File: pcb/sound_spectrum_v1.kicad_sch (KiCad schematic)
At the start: 0 parts

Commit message: feat: form pcb board as credit card-sized
feat: add esd protection ic to USB singals

fix: bug with nrst button

fix: bug with microphone connection in schematic

chore: added custom rules for board in jlcpcb
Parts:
- added C1, C12, C13, C14, C3, C6, C7, C8: 100nF, Capacitor_SMD:C_0805_2012Metric_Pad1.18x1.45mm_HandSolder, symbol Device:C
- added C10, C11: 10uF, Capacitor_SMD:C_0805_2012Metric_Pad1.18x1.45mm_HandSolder, symbol Device:C
- added C2, C4, C5, C9: 1uF, Capacitor_SMD:C_0805_2012Metric_Pad1.18x1.45mm_HandSolder, symbol Device:C
- added D2: LED, LED_SMD:LED_0805_2012Metric_Pad1.15x1.40mm_HandSolder, symbol Device:LED
- added FB1: 4.7uH, Inductor_SMD:L_0805_2012Metric_Pad1.05x1.20mm_HandSolder, symbol Device:FerriteBead
- added J1: SWD_CONN, Connector_PinHeader_2.54mm:PinHeader_2x03_P2.54mm_Vertical, symbol Connector_Generic:Conn_02x03_Counter_Clockwise
- added J2: Conn_02x10_Counter_Clockwise, Connector_PinHeader_2.54mm:PinHeader_2x10_P2.54mm_Vertical, symbol Connector_Generic:Conn_02x10_Counter_Clockwise
- added JP1: Jumper_3_Bridged12, Jumper:SolderJumper-3_P1.3mm_Bridged2Bar12_Pad1.0x1.5mm, symbol Jumper:Jumper_3_Bridged12
- added MK1-L1, MK1-R1: ICS-43434, Sensor_Audio:InvenSense_ICS-43434-6_3.5x2.65mm, symbol Sensor_Audio:ICS-43434
- added P1: USB_C_Plug_USB2.0, Connector_USB:USB_C_Receptacle_GCT_USB4085, symbol Connector:USB_C_Plug_USB2.0
- added R1: 10k, Resistor_SMD:R_0805_2012Metric_Pad1.20x1.40mm_HandSolder, symbol Device:R
- added R3: 5.1k, Resistor_SMD:R_0805_2012Metric_Pad1.20x1.40mm_HandSolder, symbol Device:R
- added R4: 1k, Resistor_SMD:R_0805_2012Metric_Pad1.20x1.40mm_HandSolder, symbol Device:R
- added R5, R6: 4.7k, Resistor_SMD:R_0805_2012Metric_Pad1.20x1.40mm_HandSolder, symbol Device:R
- added SW2: SW_DPST_x2, Button_Switch_THT:SW_PUSH_6mm, symbol Switch:SW_DPST_x2
- added U1: STM32G473CBTx, Package_QFP:LQFP-48_7x7mm_P0.5mm, symbol user_defined_libs:STM32G473CBTx
- added U2: AP2112K-3.3, Package_TO_SOT_SMD:SOT-23-5, symbol Regulator_Linear:AP2112K-3.3
- added U3: USBLC6-2SC6, Package_TO_SOT_SMD:SOT-23-6, symbol Power_Protection:USBLC6-2SC6
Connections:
- new net: D2.2 (A), R4.1
- new net: R1.1, U2.3 (EN)
- new net: P1.A5 (CC), R3.1
- new net +3.3V: C1.1, C10.1, C12.1, C13.1, C2.1, C3.1, C4.1, C5.1, C6.1, C7.1, C8.1, C9.1, FB1.1, FB1.2, J1.1 (Pin_1), J2.1 (Pin_1), J2.2 (Pin_2), J2.3 (Pin_3), JP1.3 (B), MK1-L1.5 (VDD), MK1-R1.2 (LR), MK1-R1.5 (VDD), R4.2, R5.2, R6.2, U1.1 (VBAT), U1.20 (VREF+), U1.21 (VDDA), U1.24 (VDD), U1.36 (VDD), U1.48 (VDD), U2.5 (VOUT)
- new net +5V: J2.10 (Pin_10), J2.8 (Pin_8), J2.9 (Pin_9)
- new net BOOT0: JP1.2 (C), U1.45 (PB8)
- new net GND: C1.2, C10.2, C11.2, C12.2, C13.2, C14.1, C2.2, C3.2, C4.2, C5.2, C6.2, C7.2, C8.2, C9.2, D2.1 (K), J1.3 (Pin_3), J2.11 (Pin_11), J2.4 (Pin_4), J2.5 (Pin_5), J2.6 (Pin_6), J2.7 (Pin_7), JP1.1 (A), MK1-L1.2 (LR), MK1-L1.3 (GND), MK1-R1.3 (GND), P1.A1 (GND), P1.A12 (GND), P1.B1 (GND), P1.B12 (GND), P1.S1 (SHIELD), R3.2, SW2.1 (A), U1.19 (VSSA), U1.23 (VSS), U1.35 (VSS), U1.47 (VSS), U2.2 (GND), U3.2 (GND)
- new net I2C_SCL: J2.19 (Pin_19), R6.1, U1.39 (PA15)
- new net I2C_SDA: J2.20 (Pin_20), R5.1, U1.44 (PB7)
- new net I2S_CLK: U1.27 (PB13)
- new net I2S_SCK: MK1-L1.4 (SCK), MK1-R1.4 (SCK)
- new net I2S_SD: MK1-L1.6 (SD), MK1-R1.6 (SD), U1.29 (PB15)
- new net I2S_WS: MK1-L1.1 (WS), MK1-R1.1 (WS), U1.26 (PB12)
- new net NRST: C14.2, J1.5 (Pin_5), SW2.2 (B), U1.7 (PG10)
- new net SPI_MISO: J2.17 (Pin_17), U1.14 (PA6)
- new net SPI_MOSI: J2.18 (Pin_18), U1.15 (PA7)
- new net SPI_NSS: J2.15 (Pin_15), U1.12 (PA4)
- new net SPI_SCK: J2.16 (Pin_16), U1.13 (PA5)
- new net SWCLK: J1.2 (Pin_2), U1.38 (PA14)
- new net SWDIO: J1.4 (Pin_4), U1.37 (PA13)
- new net SWO: J1.6 (Pin_6), U1.40 (PB3)
- new net UART_CK: J2.14 (Pin_14), U1.30 (PA8)
- new net UART_RX: J2.12 (Pin_12), U1.32 (PA10)
- new net UART_TX: J2.13 (Pin_13), U1.31 (PA9)
- new net USB_DM: U1.33 (PA11), U3.1 (I/O1)
- new net USB_DM_EXT: P1.A7 (D-), U3.6 (I/O1)
- new net USB_DP: U1.34 (PA12), U3.3 (I/O2)
- new net USB_DP_EXT: P1.A6 (D+), U3.4 (I/O2)
- new net VBUS: C11.1, P1.A4 (VBUS), P1.A9 (VBUS), P1.B4 (VBUS), P1.B9 (VBUS), R1.2, U2.1 (VIN), U3.5 (VBUS)
- no-connect marks 0 -> 1
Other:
- company: (none) -> Petros Athanaselis
- title: (none) -> Sound Analysis PCB

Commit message: chore: further tracing
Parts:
- JP1: value Jumper_3_Bridged12 -> BOOT_SELECT
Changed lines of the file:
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@@
 		(on_board yes)
 		(dnp no)
-		(fields_autoplaced yes)
 		(property "Reference" "C12"
 			(at 26.67 167.6399 0)
@@
 			)
 		)
-		(property "Value" "Jumper_3_Bridged12"
+		(property "Value" "BOOT_SELECT"
 			(at 29.21 93.9799 90)
 			(effects

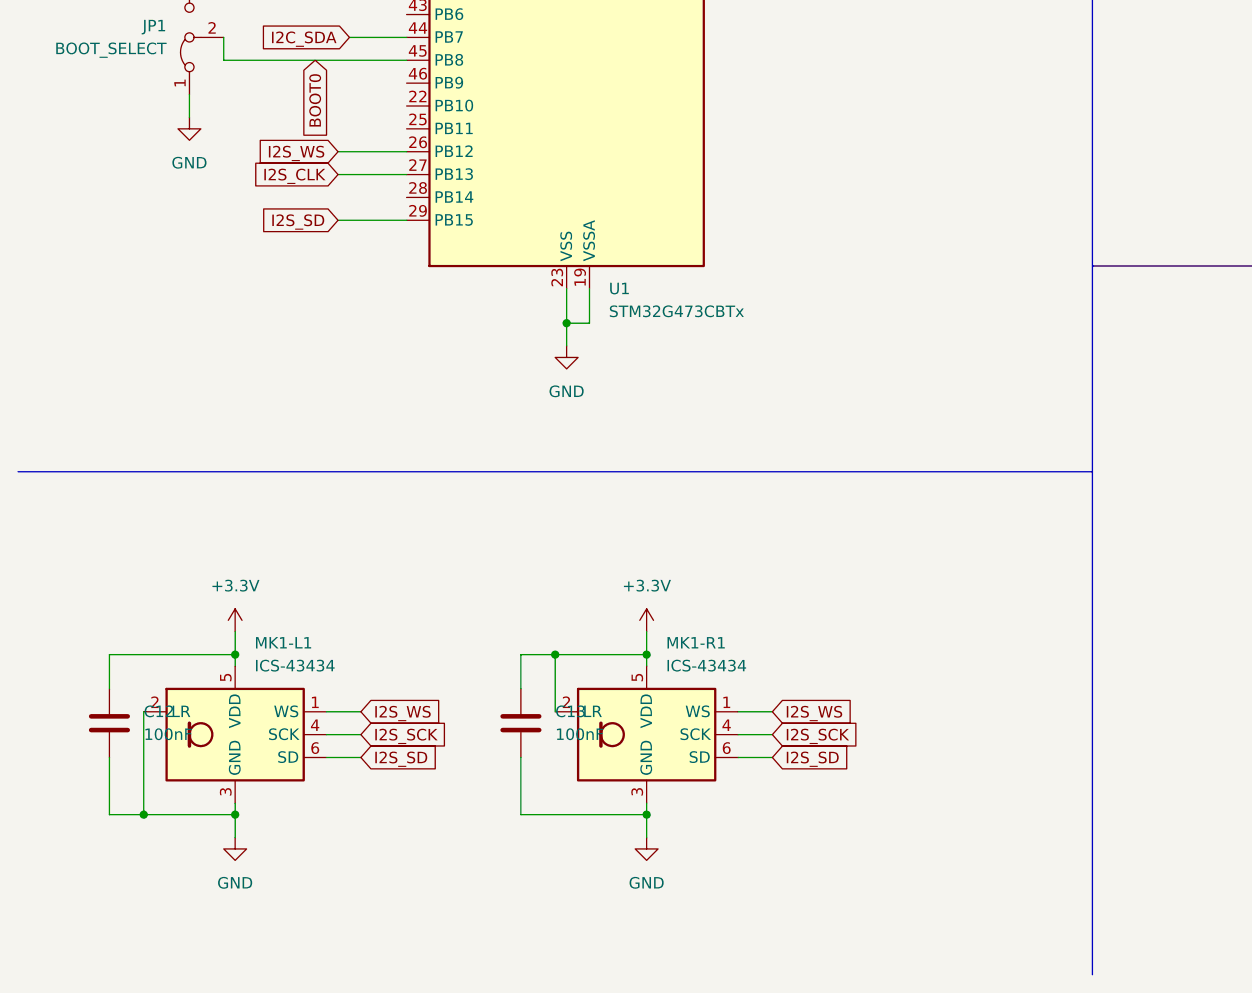
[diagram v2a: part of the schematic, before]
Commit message: fix: replace ics-43434 with ics-43432 due to part shortage
feat: make connections to all parts
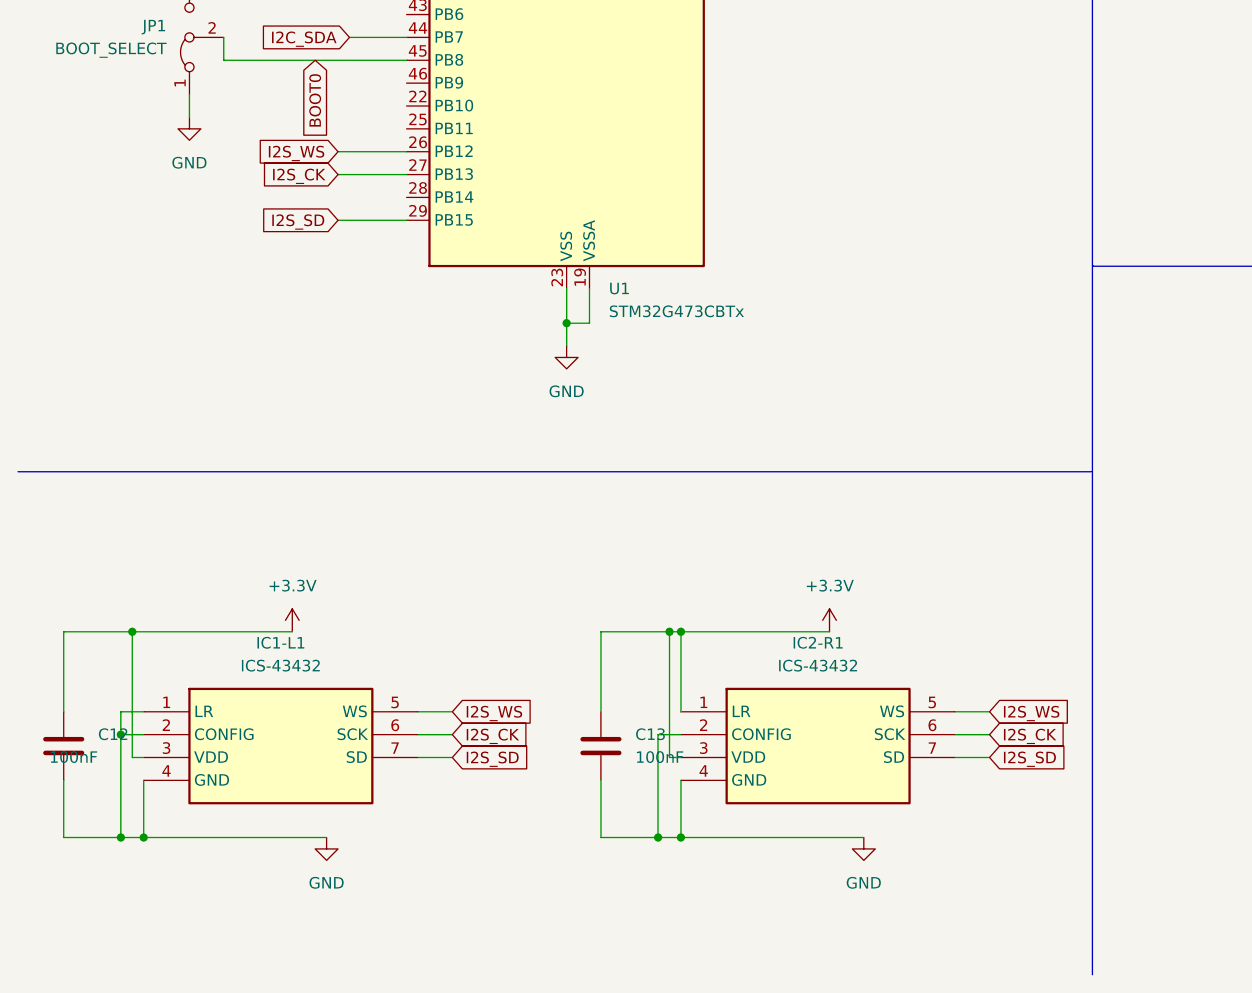
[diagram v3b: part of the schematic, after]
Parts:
- removed MK1-L1, MK1-R1: ICS-43434, Sensor_Audio:InvenSense_ICS-43434-6_3.5x2.65mm, symbol Sensor_Audio:ICS-43434
- added IC1-L1, IC2-R1: ICS-43432, ICS43432, symbol Samacsys:ICS-43432
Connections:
- net +3.3V: now also IC1-L1.3 (VDD), IC2-R1.1 (LR), IC2-R1.3 (VDD)
- net GND: now also IC1-L1.1 (LR), IC1-L1.2 (CONFIG), IC1-L1.4 (GND), IC2-R1.2 (CONFIG), IC2-R1.4 (GND)
- net I2S_SD: now also IC1-L1.7 (SD), IC2-R1.7 (SD)
- net I2S_WS: now also IC1-L1.5 (WS), IC2-R1.5 (WS)
- net I2S_CLK renamed I2S_CK
- net I2S_CK: now also IC1-L1.6 (SCK), IC2-R1.6 (SCK)
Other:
- moved on the sheet: C12, C13

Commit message: feat: add HSE clock
feat: update schematic

chore: create gerber files
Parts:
- added C15: 100nF, Capacitor_SMD:C_0805_2012Metric_Pad1.18x1.45mm_HandSolder, symbol Device:C
- added Y2: SG-210STF 48.0000ML5, Oscillator:Oscillator_SMD_SeikoEpson_SG210-4Pin_2.5x2.0mm, symbol Oscillator:SG-211
- C1, C12, C13, C14, C3, C6, C7, C8: Manufacturer_Part_Number (none) -> 581-KGM21NR71E104KM
- C10, C11: Manufacturer_Part_Number (none) -> 81-GRM21BR61C106KE15
- C2, C4, C5, C9: Manufacturer_Part_Number (none) -> 80-C0805C105Z4VAC
- D2: Manufacturer_Part_Number (none) -> CMDA5AR7D1S
- FB1: Manufacturer_Part_Number (none) -> ASMPH-0805-4R7M-T
- J1: Manufacturer_Part_Number (none) -> 10129381-906004BLF
- J2: Manufacturer_Part_Number (none) -> 77313-818-20LF
- P1: Manufacturer_Part_Number (none) -> USB4085-GF-A
- R1: Manufacturer_Part_Number (none) -> 603-AC0805DR-0710KL
- R3: Manufacturer_Part_Number (none) -> CRCW08055K10JNEA
- R4: Manufacturer_Part_Number (none) -> 603-AA0805FR-071KL
- R5, R6: Manufacturer_Part_Number (none) -> 603-RC0805FR-074K7L
- SW2: Manufacturer_Part_Number (none) -> TS04-66-55-BK-100-SMT-TR
- U1: Manufacturer_Part_Number (none) -> STM32G473CBT6
- U2: Manufacturer_Part_Number (none) -> AP2112K-3.3TRG1
- U3: Manufacturer_Part_Number (none) -> USBLC6-2SC6
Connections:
- net +3.3V: now also C15.1, Y2.1 (~{ST}), Y2.4 (Vcc)
- net GND: now also C15.2, Y2.2 (GND)
- net at U1.5 (PF0): now also Y2.3 (OUT)
- no-connect marks 1 -> 19

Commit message: chore: generated cpl file
fix: errors in schematic
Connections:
- net +5V is gone; now on net VBUS: J2.10 (Pin_10), J2.8 (Pin_8), J2.9 (Pin_9)
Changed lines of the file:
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@@
 	)
 	(junction
+		(at 256.54 21.59)
+		(diameter 0)
+		(color 0 0 0 0)
+	)
+	(junction
 		(at 207.01 38.1)
 		(diameter 0)
@@
 	)
 	(junction
+		(at 240.03 60.96)
+		(diameter 0)
+		(color 0 0 0 0)
+	)
+	(junction
 		(at 46.99 29.21)
 		(diameter 0)
@@
 	(wire
 		(pts
+			(xy 237.49 60.96) (xy 240.03 60.96)
+		)
+		(stroke
+			(width 0)
+			(type default)
+		)
+	)
+	(wire
+		(pts
 			(xy 99.06 19.05) (xy 99.06 21.59)
 		)
@@
 	(wire
 		(pts
-			(xy 240.03 59.69) (xy 240.03 62.23)
+			(xy 240.03 59.69) (xy 240.03 60.96)
 		)
 		(stroke
@@
 	(wire
 		(pts
+			(xy 256.54 21.59) (xy 261.62 21.59)
+		)
+		(stroke
+			(width 0)
+			(type default)
+		)
+	)
+	(wire
+		(pts
 			(xy 31.75 99.06) (xy 31.75 101.6)
 		)
@@
 	(wire
 		(pts
+			(xy 240.03 60.96) (xy 240.03 62.23)
+		)
+		(stroke
+			(width 0)
+			(type default)
+		)
+	)
+	(wire
+		(pts
 			(xy 91.44 57.15) (xy 99.06 57.15)
 		)
@@
 	(wire
 		(pts
-			(xy 255.27 21.59) (xy 261.62 21.59)
+			(xy 255.27 21.59) (xy 256.54 21.59)
 		)
 		(stroke
@@
 	(wire
 		(pts
+			(xy 256.54 20.32) (xy 256.54 21.59)
+		)
+		(stroke
+			(width 0)
+			(type default)
+		)
+	)
+	(wire
+		(pts
 			(xy 254 95.25) (xy 254 97.79)
 		)
@@
 		)
 	)
+	(global_label "VBUS"
+		(shape input)
+		(at 212.09 110.49 90)
+		(fields_autoplaced yes)
+		(effects
+			(font
+				(size 1.27 1.27)
+			)
+			(justify left)
+		)
+		(property "Intersheetrefs" "${INTERSHEET_REFS}"
+			(at 212.09 102.6062 90)
+			(effects
+				(font
+					(size 1.27 1.27)
+				)
+				(justify left)
+				(hide yes)
+			)
+		)
+	)
 	(global_label "I2C_SCL"
 		(shape input)
@@
 	)
 	(symbol
-		(lib_id "power:+3.3V")
-		(at 212.09 110.49 0)
-		(unit 1)
-		(exclude_from_sim no)
-		(in_bom yes)
-		(on_board yes)
-		(dnp no)
-		(fields_autoplaced yes)
-		(property "Reference" "#PWR029"
-			(at 212.09 114.3 0)
-			(effects
-				(font
-					(size 1.27 1.27)
-				)
-				(hide yes)
-			)
-		)
-		(property "Value" "+5V"
-			(at 212.09 105.41 0)
-			(effects
-				(font
-					(size 1.27 1.27)
-				)
-			)
-		)
-		(property "Footprint" ""
-			(at 212.09 110.49 0)
-			(effects
-				(font
-					(size 1.27 1.27)
-				)
-				(hide yes)
-			)
-		)
-		(property "Datasheet" ""
-			(at 212.09 110.49 0)
-			(effects
-				(font
-					(size 1.27 1.27)
-				)
-				(hide yes)
-			)
-		)
-		(property "Description" "Power symbol creates a global label with name \"+3.3V\""
-			(at 212.09 110.49 0)
-			(effects
-				(font
-					(size 1.27 1.27)
-				)
-				(hide yes)
-			)
-		)
-		(pin "1"
-		)
-		(instances
-			(project "sound_spectrum_v1"
-				(path "/e63e39d7-6ac0-4ffd-8aa3-1841a4541b55"
-					(reference "#PWR029")
-					(unit 1)
-				)
-			)
-		)
-	)
-	(symbol
 		(lib_id "power:GND")
 		(at 240.03 62.23 0)
@@
 	)
 	(symbol
+		(lib_id "power:PWR_FLAG")
+		(at 256.54 20.32 0)
+		(unit 1)
+		(exclude_from_sim no)
+		(in_bom yes)
+		(on_board yes)
+		(dnp no)
+		(fields_autoplaced yes)
+		(property "Reference" "#FLG01"
+			(at 256.54 18.415 0)
+			(effects
+				(font
+					(size 1.27 1.27)
+				)
+				(hide yes)
+			)
+		)
+		(property "Value" "PWR_FLAG"
+			(at 256.54 15.24 0)
+			(effects
+				(font
+					(size 1.27 1.27)
+				)
+			)
+		)
+		(property "Footprint" ""
+			(at 256.54 20.32 0)
+			(effects
+				(font
+					(size 1.27 1.27)
+				)
+				(hide yes)
+			)
+		)
+		(property "Datasheet" "~"
+			(at 256.54 20.32 0)
+			(effects
+				(font
+					(size 1.27 1.27)
+				)
+				(hide yes)
+			)
+		)
+		(property "Description" "Special symbol for telling ERC where power comes from"
+			(at 256.54 20.32 0)
+			(effects
+				(font
+					(size 1.27 1.27)
+				)
+				(hide yes)
+			)
+		)
+		(pin "1"
+		)
+		(instances
+			(project ""
+				(path "/e63e39d7-6ac0-4ffd-8aa3-1841a4541b55"
+					(reference "#FLG01")
+					(unit 1)
+				)
+			)
+		)
+	)
+	(symbol
 		(lib_id "Device:C")
 		(at 35.56 43.18 0)
@@
 					(unit 1)
 				)
+			)
+		)
+	)
+	(symbol
+		(lib_id "power:PWR_FLAG")
+		(at 237.49 60.96 90)
+		(unit 1)
+		(exclude_from_sim no)
+		(in_bom yes)
+		(on_board yes)
+		(dnp no)
+		(fields_autoplaced yes)
+		(property "Reference" "#FLG02"
+			(at 235.585 60.96 0)
+			(effects
+				(font
+					(size 1.27 1.27)
+				)
+				(hide yes)
+			)
+		)
+		(property "Value" "PWR_FLAG"
+			(at 233.68 60.9599 90)
+			(effects
+				(font
+					(size 1.27 1.27)
+				)
+				(justify left)
+			)
+		)
+		(property "Footprint" ""
+			(at 237.49 60.96 0)
+			(effects
+				(font
+					(size 1.27 1.27)
+				)
+				(hide yes)
+			)
+		)
+		(property "Datasheet" "~"
+			(at 237.49 60.96 0)
+			(effects
+				(font
+					(size 1.27 1.27)
+				)
+				(hide yes)
+			)
+		)
+		(property "Description" "Special symbol for telling ERC where power comes from"
+			(at 237.49 60.96 0)
+			(effects
+				(font
+					(size 1.27 1.27)
+				)
+				(hide yes)
+			)
+		)
+		(pin "1"
+		)
+		(instances
+			(project ""
+				(path "/e63e39d7-6ac0-4ffd-8aa3-1841a4541b55"
+					(reference "#FLG02")
+					(unit 1)
+				)
